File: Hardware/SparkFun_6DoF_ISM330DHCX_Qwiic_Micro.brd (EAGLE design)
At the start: 25.4 x 12.7 mm, 46 parts, among them J1 Qwiic Right Angle, U1 ISM330DHCX

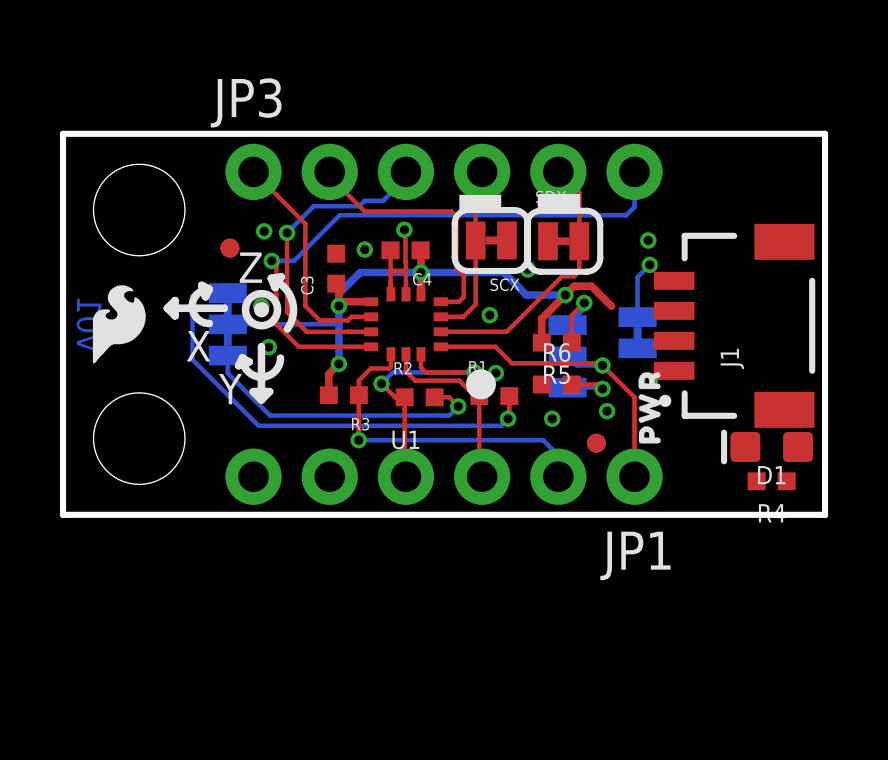
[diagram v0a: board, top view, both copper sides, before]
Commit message: Adds a save point for Qwiic Micro - Revert here if removing SPI is not
the way.
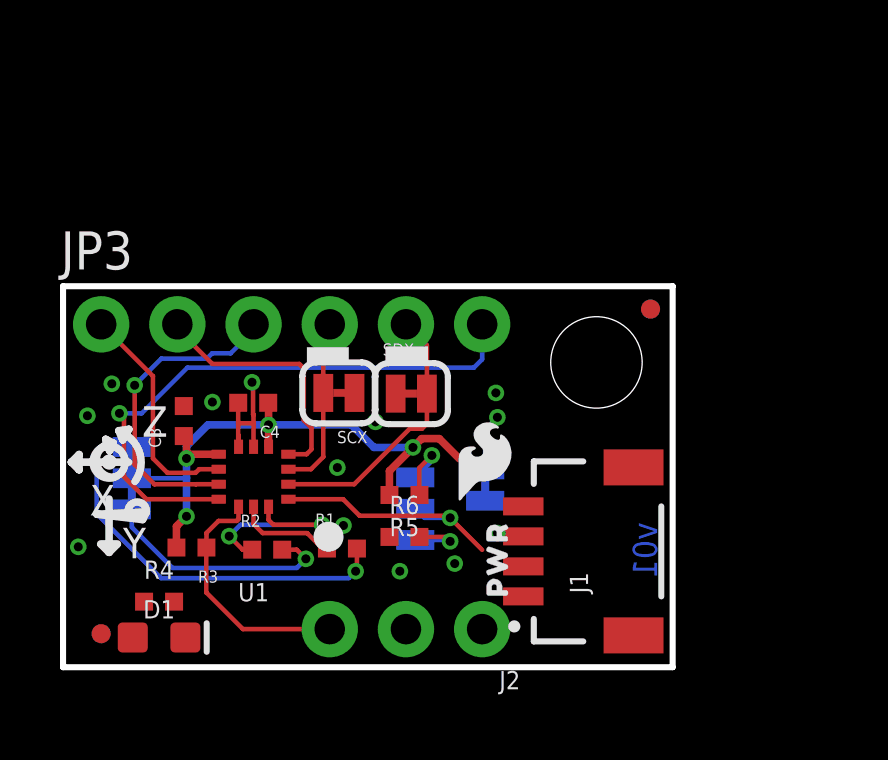
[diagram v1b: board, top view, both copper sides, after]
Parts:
- removed JP1: IO, SparkFun-Connectors:1X06_NO_SILK
- removed STANDOFF2: STAND-OFFTIGHT, SparkFun-Hardware:STAND-OFF-TIGHT
- removed U$37: (no value), ISMTopMini:SCL5
- removed U$40: (no value), ISMTopMini:SDA6
- added J2: (no value), SparkFun-Connectors:1X03_NO_SILK
- moved D1 21.4 mm to (3.20, 0.99), turned to 0 degrees
- moved R4 20.8 mm to (3.20, 2.18), turned to 0 degrees
- moved LOGO2 17.8 mm to (17.9, 3.74)
- moved FD2 17.7 mm to (1.27, 1.12)
- moved FID2 17.7 mm to (1.27, 1.12)
- moved STANDOFF1 16.1 mm to (17.8, 10.2)
- moved FD1 14.2 mm to (19.6, 11.9)
- moved FID1 14.2 mm to (19.6, 11.9)
- moved U$29 13.0 mm to (14.0, 6.88)
- moved U$39 9.46 mm to (11.5, 2.74), turned to 180 degrees
- moved U$42 9.21 mm to (14.1, 3.40)
- moved J1 9.05 mm to (15.3, 3.86)
- moved U$38 8.10 mm to (8.94, 3.00)
- moved JP3 7.18 mm to (1.27, 11.4)
- moved U$35 7.18 mm to (11.4, 9.09)
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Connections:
- net !CS!: now also J2.3; no longer JP1.2
- net GND: now also J2.1; no longer JP1.6
- net SDO/SA0: now also J2.2; no longer JP1.1
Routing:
- net !CS!: track 11.2 -> 8.28 mm, vias 1 -> 0
- net SDO/SA0: track 11.1 -> 8.45 mm
- net SDA: track 9.11 -> 6.51 mm
- net SCL: track 5.95 -> 3.36 mm
- net N$6: track 9.89 -> 7.99 mm
- net N$5: track 15.6 -> 13.7 mm
- net 3.3V: track 22.6 -> 20.7 mm
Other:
- board size 25.4 x 12.7 mm -> 20.3 x 12.7 mm

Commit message: Removes Auxiliary pins to make the Qwiic Micro as Micro as possible
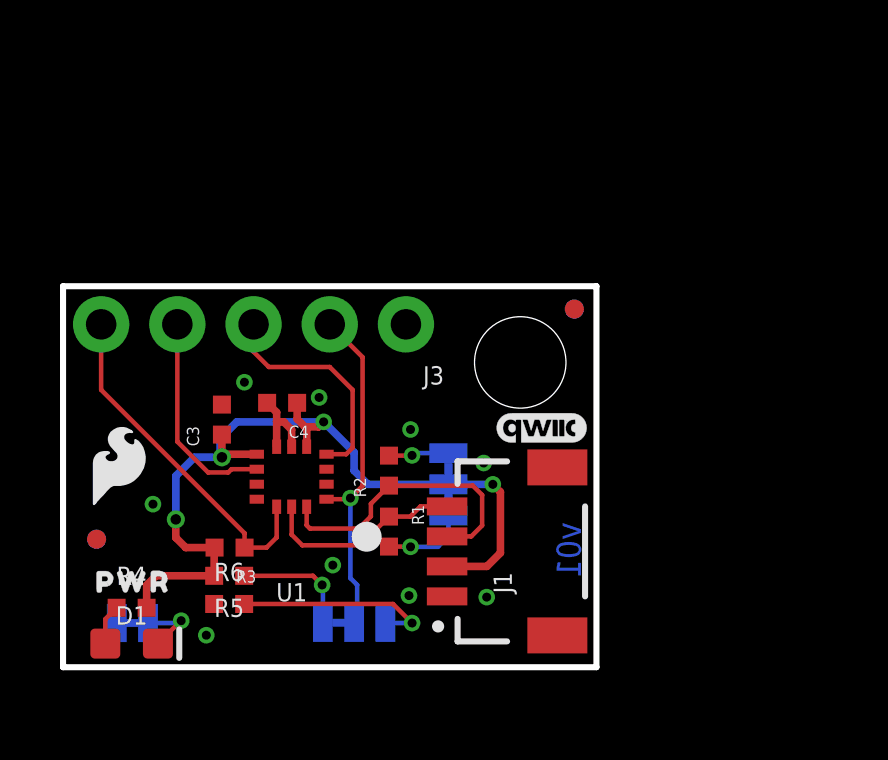
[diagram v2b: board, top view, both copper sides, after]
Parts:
- removed J2: (no value), SparkFun-Connectors:1X03_NO_SILK
- removed JP3: IO, SparkFun-Connectors:1X06_NO_SILK
- removed SCX, SDX: JUMPER-SMT_2_NC_TRACE_SILK, SparkFun-Jumpers:SMT-JUMPER_2_NC_TRACE_SILK
- removed U$34: (no value), ISMTopMini:SDOX9
- removed U$35: (no value), ISMTopMini:SDIX8
- removed U$36: (no value), ISMTopMini:SCX7
- removed U$41: (no value), ISMTopMini:3V30
- removed U$43: (no value), ISMTopMini:OCS2112
- added J3: (no value), SparkFun-Connectors:1X05_NO_SILK
- added LOGO1: QWIIC_LOGO_3MM, SparkFun-Aesthetics:QWIIC_3MM
- added LOGO3: SFE_LOGO_NAME_FLAMEBLANK, SparkFun-Aesthetics:BLANK
- moved U$25 13.8 mm to (14.5, 6.22), turned to 90 degrees
- moved LED 12.6 mm to (2.31, 1.47), turned to 180 degrees
- moved U$29 12.2 mm to (1.85, 6.73)
- moved U$28 12.2 mm to (2.34, 2.84), turned to 0 degrees
- moved I2C_PU 10.6 mm to (12.8, 6.10), turned to 90 degrees
- moved U$38 9.96 mm to (1.27, 9.35), turned to 90 degrees
- moved U$16 7.96 mm to (2.34, 3.07)
- moved U$39 6.78 mm to (8.89, 8.99), turned to 90 degrees
- moved R5 6.43 mm to (5.54, 3.05)
- moved U$42 6.34 mm to (11.5, 9.19), turned to 90 degrees
- moved R6 6.26 mm to (5.54, 2.11)
- moved LOGO2 5.11 mm to (13.3, 1.45)
- moved R2 4.84 mm to (10.9, 6.55), turned to 90 degrees
- moved ADDR 4.32 mm to (9.70, 1.48), turned to 0 degrees
- moved FD2 3.15 mm to (1.12, 4.27)
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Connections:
- net SDA renamed SDA/PICO
- removed net OCS: JP3.3, U1.P10
- removed net SCX: JP3.4, SCX.2, U1.P3
- removed net SDI_AUX: JP3.5, SDX.2, U1.P2
- removed net SDO/SA0: ADDR.2, J2.2, U1.P1
- removed net SDO_AUX: JP3.6, U1.P11
- new net POCI/SA0: ADDR.2, J3.2, U1.P1
- net !CS!: now also J3.5; no longer J2.3
- net GND: now also J3.1; no longer J2.1, SCX.1, SDX.1
- net INT1: now also J3.3; no longer JP3.2
- net INT2: now also J3.4; no longer JP3.1
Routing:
- net SDO_AUX: track 19.6 -> 0.00 mm, vias 1 -> 0
- net POCI/SA0: track 0.00 -> 11.5 mm, vias 0 -> 1
- net N$5: track 13.7 -> 2.82 mm
- net OCS: track 10.6 -> 0.00 mm, vias 1 -> 0
- net SDI_AUX: track 9.05 -> 0.00 mm
- net SDO/SA0: track 8.45 -> 0.00 mm, vias 1 -> 0
- net 3.3V: track 20.7 -> 29.1 mm
- net N$6: track 7.99 -> 2.02 mm
- net SCX: track 5.84 -> 0.00 mm
- net N$7: track 2.27 -> 6.75 mm
- net SCL: track 3.36 -> 6.80 mm
- net !CS!: track 8.28 -> 11.7 mm
- net SDA/PICO: track 6.51 -> 9.82 mm, vias 2 -> 0
- net N$1: track 2.46 -> 4.00 mm
- net GND: track 4.21 -> 2.77 mm, vias 12 -> 9
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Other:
- board size 20.3 x 12.7 mm -> 17.8 x 12.7 mm
- board text removed: "X"
- board text removed: "Y"
- board text removed: "Z"
